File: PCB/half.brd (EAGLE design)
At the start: 135.6 x 90.2 mm, 144 parts, among them J10 AUDIO_JACK_TRRSSMD_RA, J7 AUDIO_JACK_TRRSSMD_RA, J8 AUDIO_JACK_TRRSSMD_RA, J9 AUDIO_JACK_TRRSSMD_RA

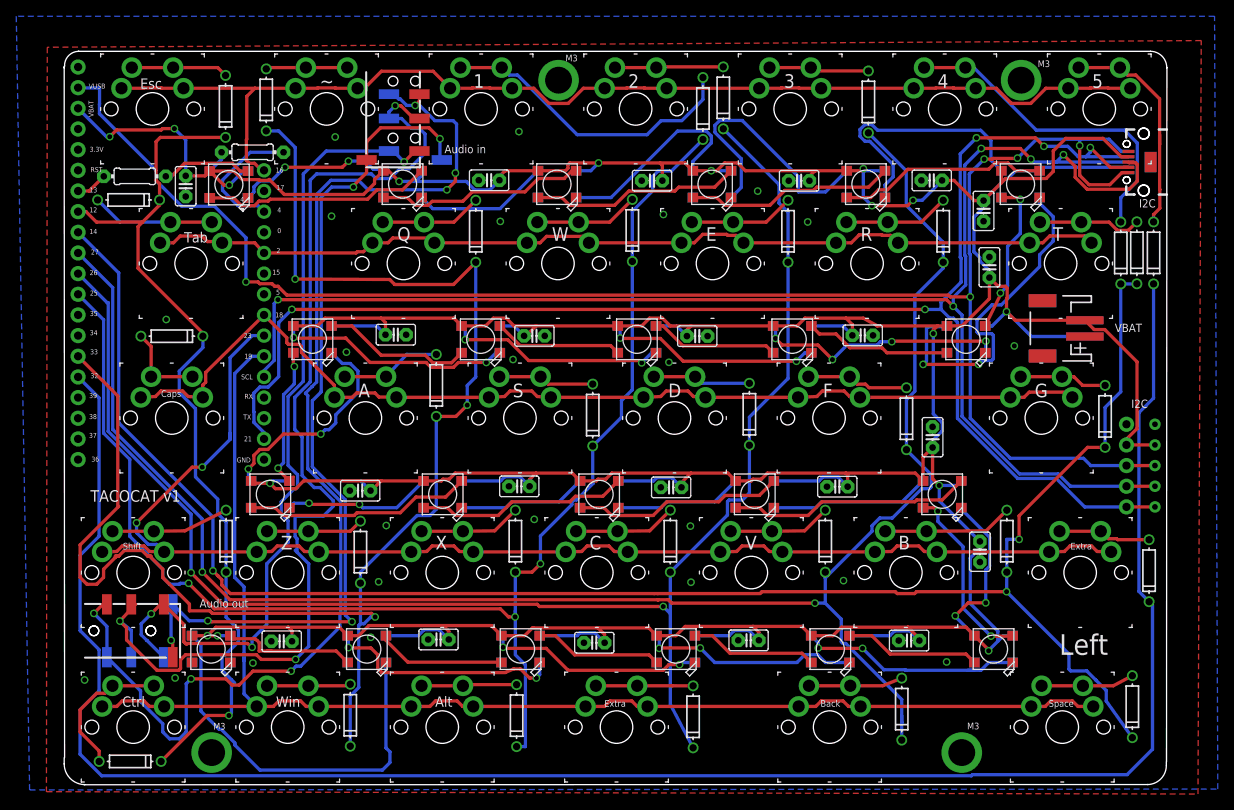
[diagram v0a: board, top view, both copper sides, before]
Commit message: PCB update, improved micro usb part with longer pads, capacitor added to VBAT circuit
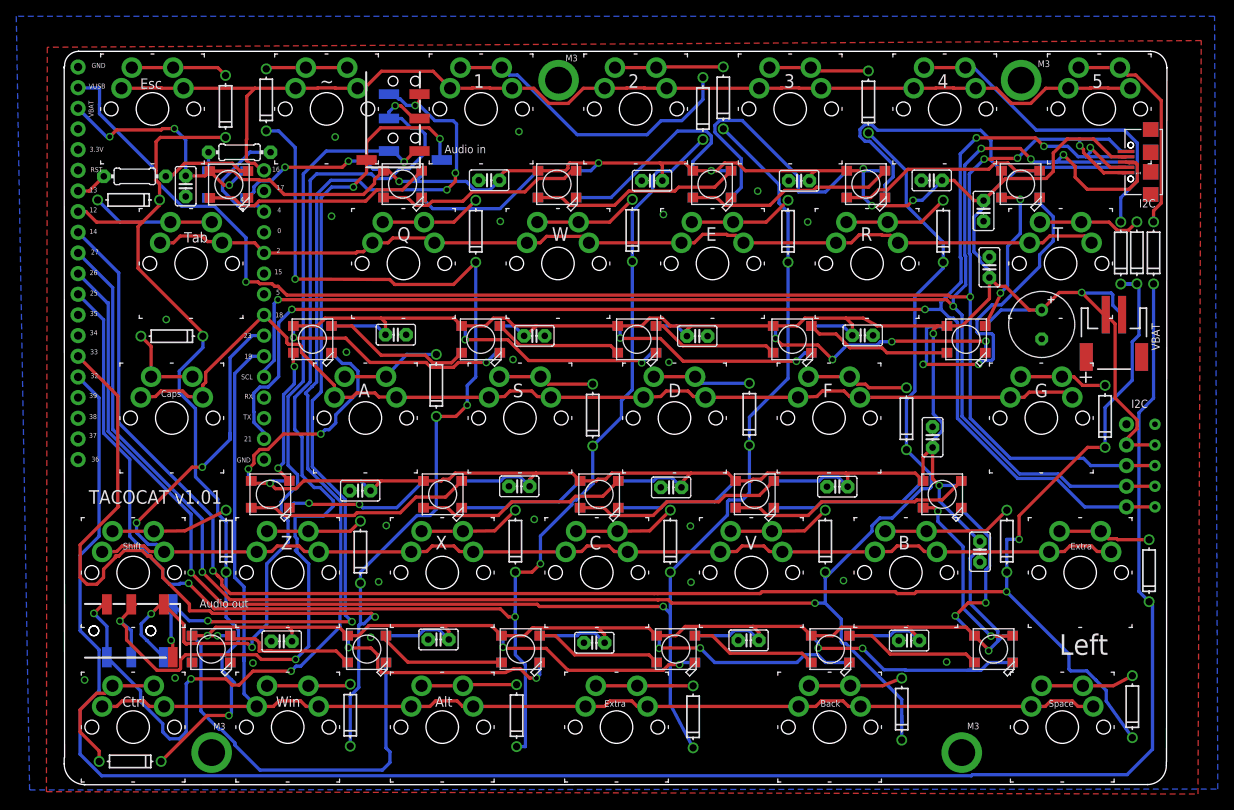
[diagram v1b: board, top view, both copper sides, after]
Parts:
- added C17: 1000uF, adafruit:E3,5-8
- J3, J5: device SparkFun-Connectors:USB-B-MICRO-SMD-HOLES -> EAGLE-INPUT_OUTPUT_CONNECTORS-rev17a:629105136821
- moved J11 7.55 mm to (129.0, 54.1), turned to 180 degrees
- moved J4 7.55 mm to (129.0, 54.1), turned to 180 degrees
- moved R2 1.60 mm to (21.5, 77.7)
- moved LED23 0.30 mm to (19.9, 73.8)
- turned J3 to 270 degrees
- turned J5 to 90 degrees
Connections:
- net GND: now also C17.-, J3.5, J5.5; no longer J3.GND, J5.GND
- net SCL: now also J3.3, J5.3; no longer J3.D+, J5.D+
- net SDA: now also J3.2, J5.2; no longer J3.D-, J5.D-
- net VBAT: now also C17.+, J3.4, J5.4; no longer J3.ID, J5.ID
- net VUSB: now also J3.1, J5.1; no longer J3.VBUS, J5.VBUS
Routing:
- net VUSB: track 214.8 -> 211.7 mm
- net C6: track 220.9 -> 223.4 mm
- net 4: track 16.4 -> 14.8 mm
- net N$7: track 28.2 -> 27.1 mm
- net VBAT: track 713.1 -> 714.0 mm
- net SDA: track 191.8 -> 191.2 mm
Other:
- board text added: "TACOCAT v1.01"
- board text removed: "TACOCAT v1"

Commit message: pcb update
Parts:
- J3, J5: value (none) -> USB_MINI-B_SMT; device EAGLE-INPUT_OUTPUT_CONNECTORS-rev17a:629105136821 -> SparkFun-Connectors:USB-MINIB
- LED1, LED10, LED11, LED12, LED13, LED14, LED15, LED16, LED17, LED18, LED19, LED2, LED20, LED21, LED22, LED23, LED24, LED25, LED26, LED27, LED28, LED29, LED3, LED30, LED31, LED32, LED33, LED34, LED35, LED36, LED37, LED38, LED39, LED4, LED40, LED41, LED42, LED43, LED44, LED5, LED6, LED7, LED8, LED9: value WS2812B_5050N -> WS2812BLONGPADS; device adafruit:WS2812B-NARROW -> adafruit:WS2812B-NARROW-PADS
- moved C17 90.9 mm to (32.1, 79.5), turned to 0 degrees
- moved D29 29.9 mm to (37.5, 8.54), turned to 270 degrees
- moved J11 7.01 mm to (122.4, 56.5), turned to 270 degrees
- moved J4 7.01 mm to (122.4, 56.5), turned to 90 degrees
- moved J3 3.03 mm to (130.9, 75.1), turned to 0 degrees
- moved J5 3.03 mm to (130.9, 75.1), turned to 180 degrees
- moved D13 1.17 mm to (131.8, 64.2)
- moved D7 1.16 mm to (133.9, 64.2)
- moved D6 1.15 mm to (129.8, 64.2)
- moved C6 0.93 mm to (113.0, 69.6)
- moved LED1 0.60 mm to (19.6, 73.8)
- moved LED23 0.30 mm to (19.6, 73.8)
- moved LED18 0.12 mm to (41.5, 73.7)
- moved LED40 0.12 mm to (41.5, 73.7)
- moved C11 0.09 mm to (14.8, 73.6)
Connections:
- net GND: now also J3.GND, J5.GND; no longer J3.5, J5.5
- net SCL: now also J3.D+, J5.D+; no longer J3.3, J5.3
- net SDA: now also J3.D-, J5.D-; no longer J3.2, J5.2
- net VBAT: now also J3.ID, J5.ID; no longer J3.4, J5.4
- net VUSB: now also J3.VBUS, J5.VBUS; no longer J3.1, J5.1
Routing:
- net N$6: track 17.6 -> 62.2 mm, vias 0 -> 1
- net N$36: track 133.7 -> 154.2 mm, vias 3 -> 6
- net SCL: track 191.0 -> 176.9 mm, vias 5 -> 6
- net C1: track 109.3 -> 119.2 mm, vias 1 -> 0
- net N$27: track 40.8 -> 45.9 mm, vias 0 -> 1
- net N$7: track 27.1 -> 32.1 mm
- net N$33: track 28.2 -> 33.1 mm
- net R1: track 172.6 -> 176.8 mm
- net N$44: track 145.5 -> 141.8 mm
- net N$81: track 32.2 -> 35.7 mm
- net SDA: track 191.2 -> 194.6 mm, vias 5 -> 6
- net VBAT: track 714.0 -> 717.3 mm, vias 16 -> 17
- net GND: track 0.00 -> 3.13 mm, vias 22 -> 34
- net N$67: track 49.0 -> 51.6 mm
- net N$16: track 37.7 -> 40.2 mm
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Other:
- board text added: "22"
- board text removed: "SCL"
